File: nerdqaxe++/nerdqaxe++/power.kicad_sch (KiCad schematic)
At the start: 60 parts, among them J3 Conn_01x01, J4 Conn_01x01, U3 TPS53647, U36 MCP1824T-1202E, U6 AP3211, U7 MCP1824T-0802E

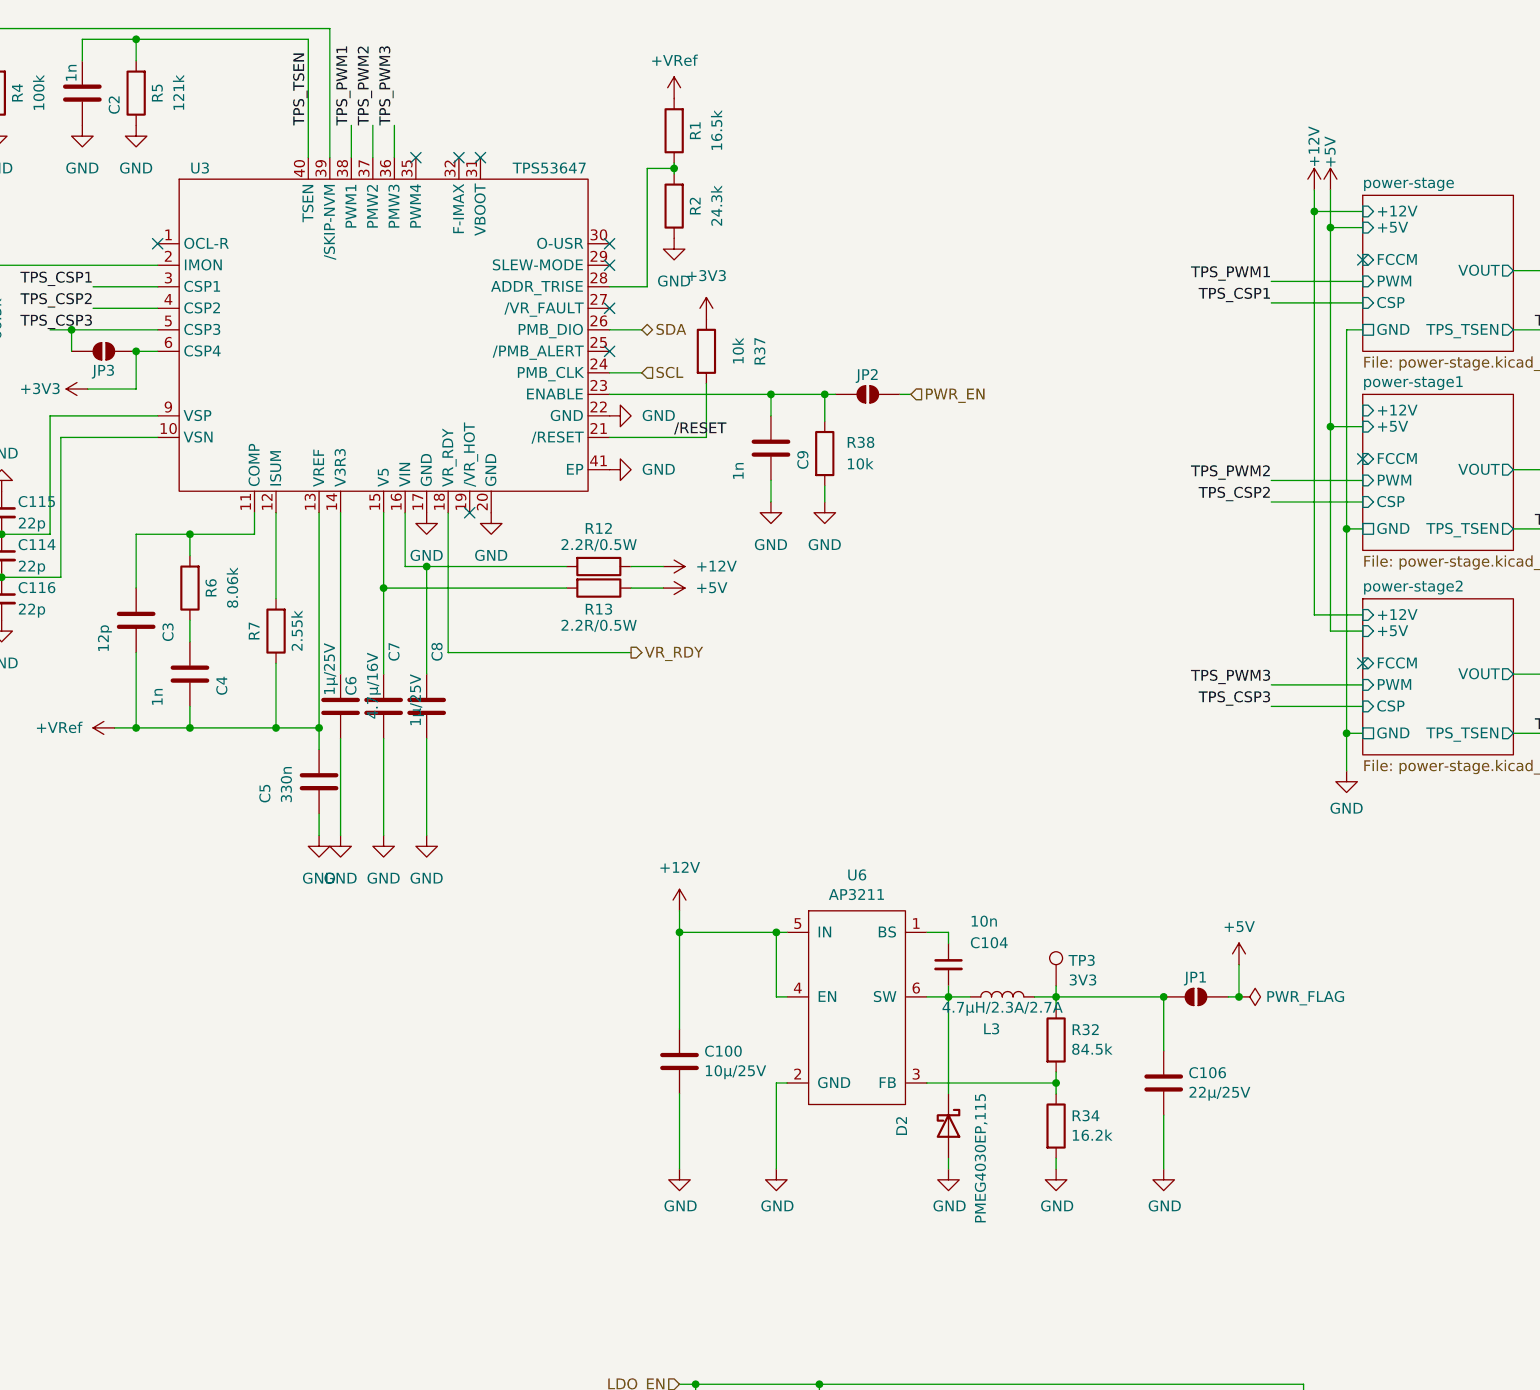
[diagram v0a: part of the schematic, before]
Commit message: Updated PCB layout
- Replaced barrel jack socket with XT30M
- Replaced old fuse holder with new 3568
- Reordered components for AP3211 5V buck converter
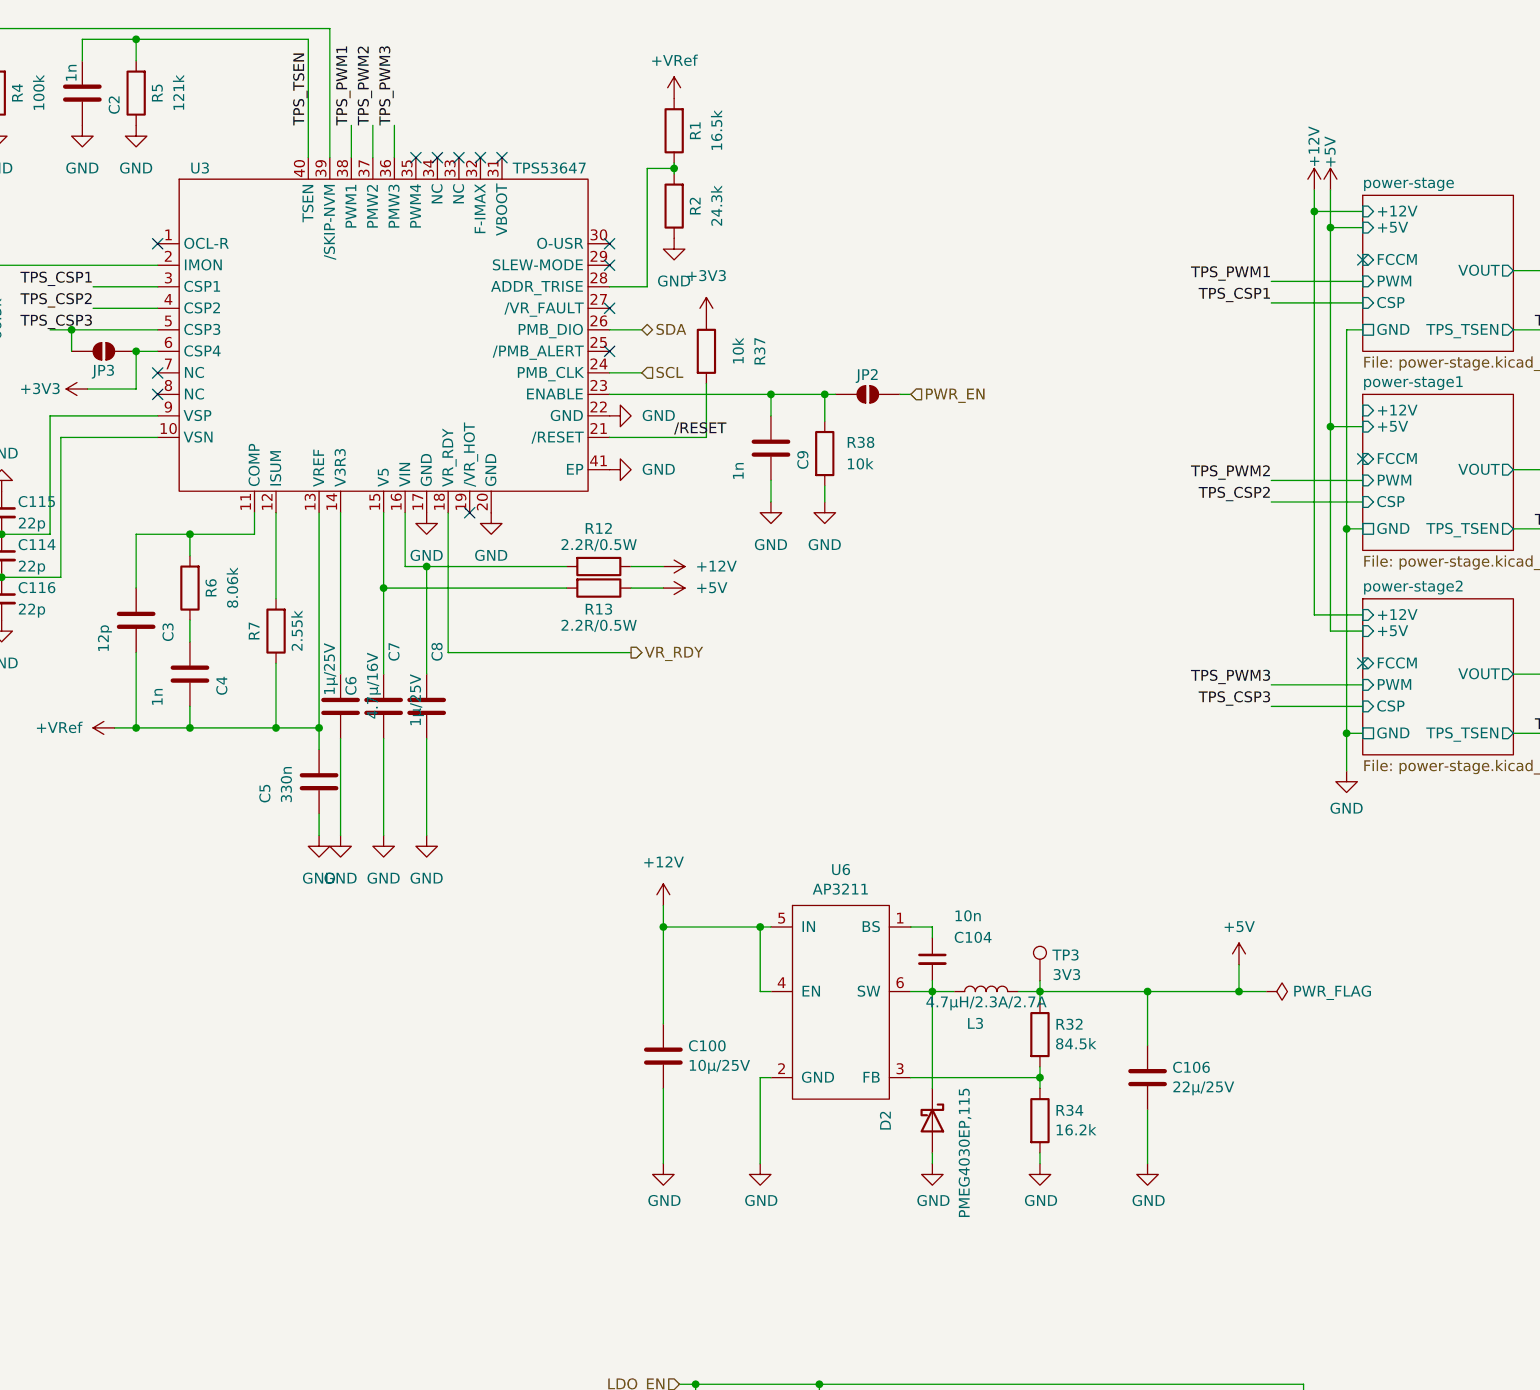
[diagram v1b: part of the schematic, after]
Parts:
- removed JP1: SolderJumper_2_Open, Jumper:SolderJumper-2_P1.3mm_Open_RoundedPad1.0x1.5mm, symbol Jumper:SolderJumper_2_Open
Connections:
- net +5V: now also C106.1, L3.2, R32.1, TP3.1
- no-connect marks 14 -> 18
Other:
- moved on the sheet: C100, C104, C106, D2, L3, R32, R34, TP3, U6

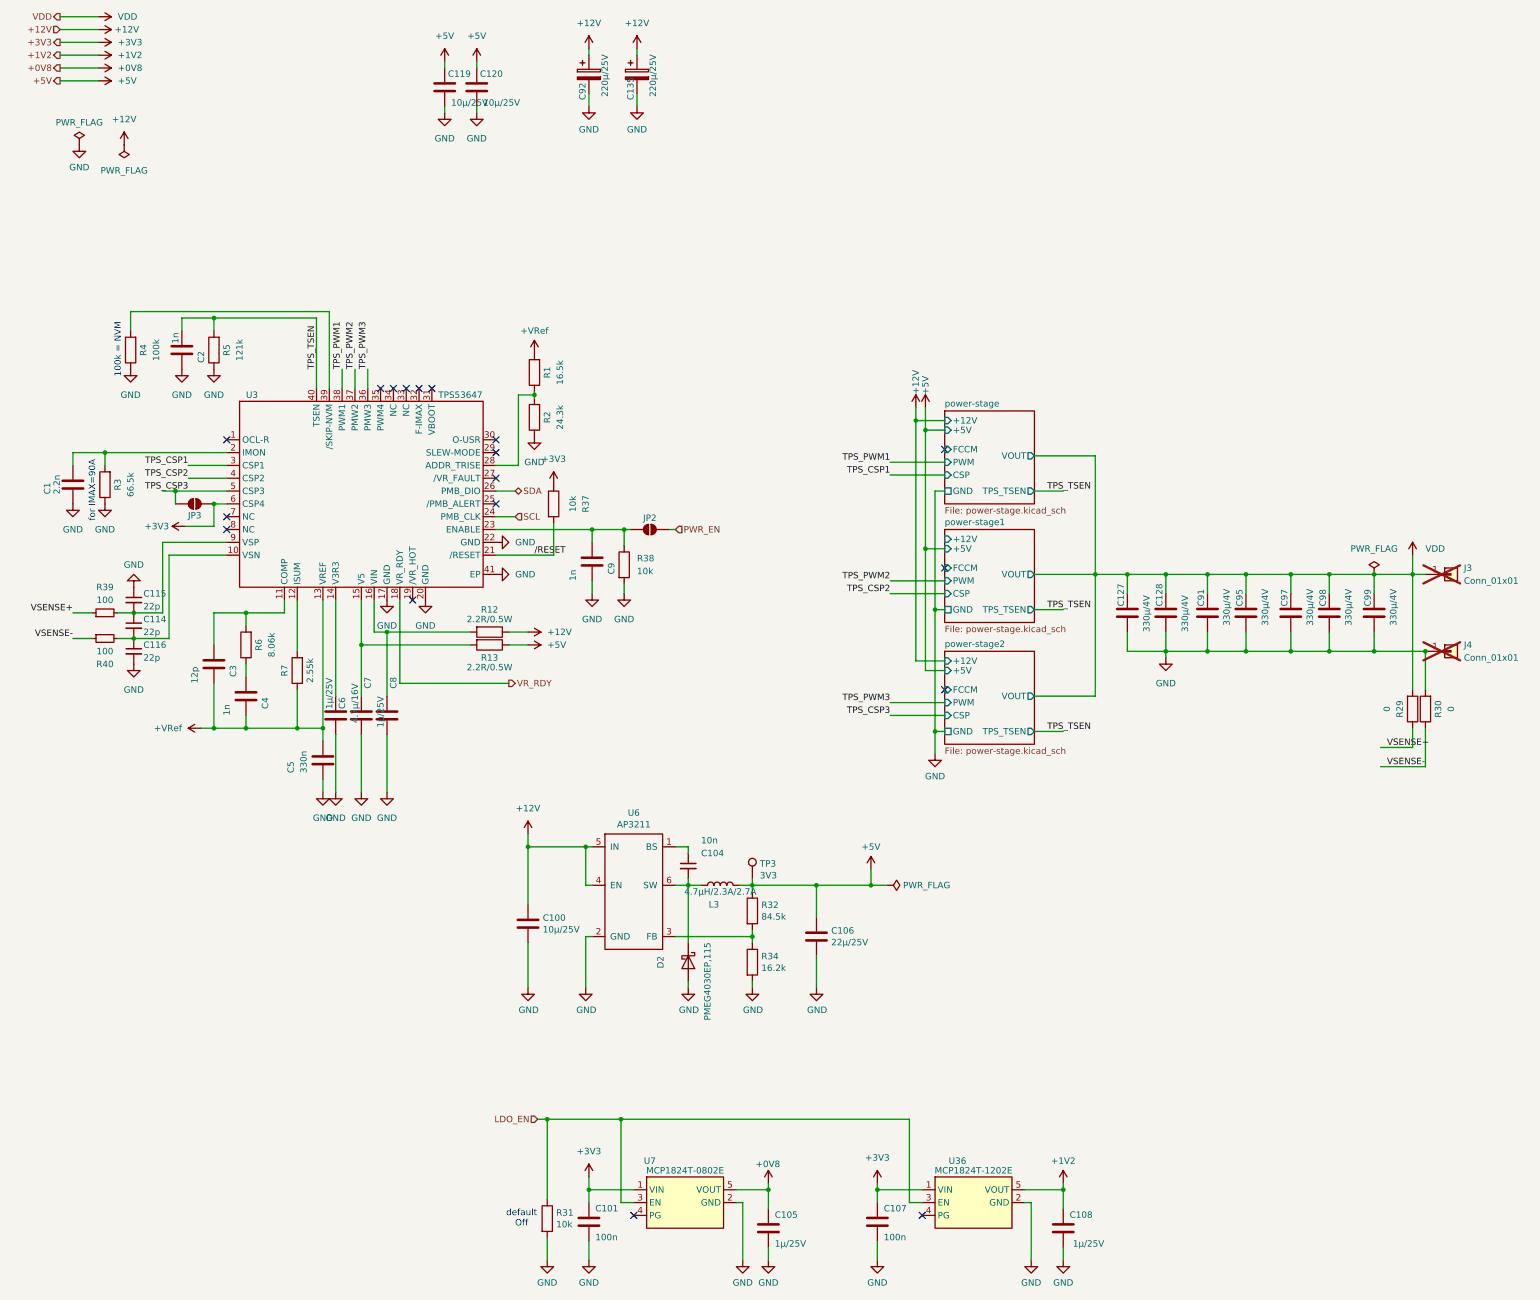
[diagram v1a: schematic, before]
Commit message: Nerdqaxe++ rev6.1.2PM
1. BM1370 Footprint solder paste revision
2. Added 2R2 resistor in series with bootstrap cap for CSD95472Q5MC
3. 180nH inductors for CSD
4. Vsense closer to ASICs
5. Fiducials
6. Updated top silkscreen
7. Various changes in tracing
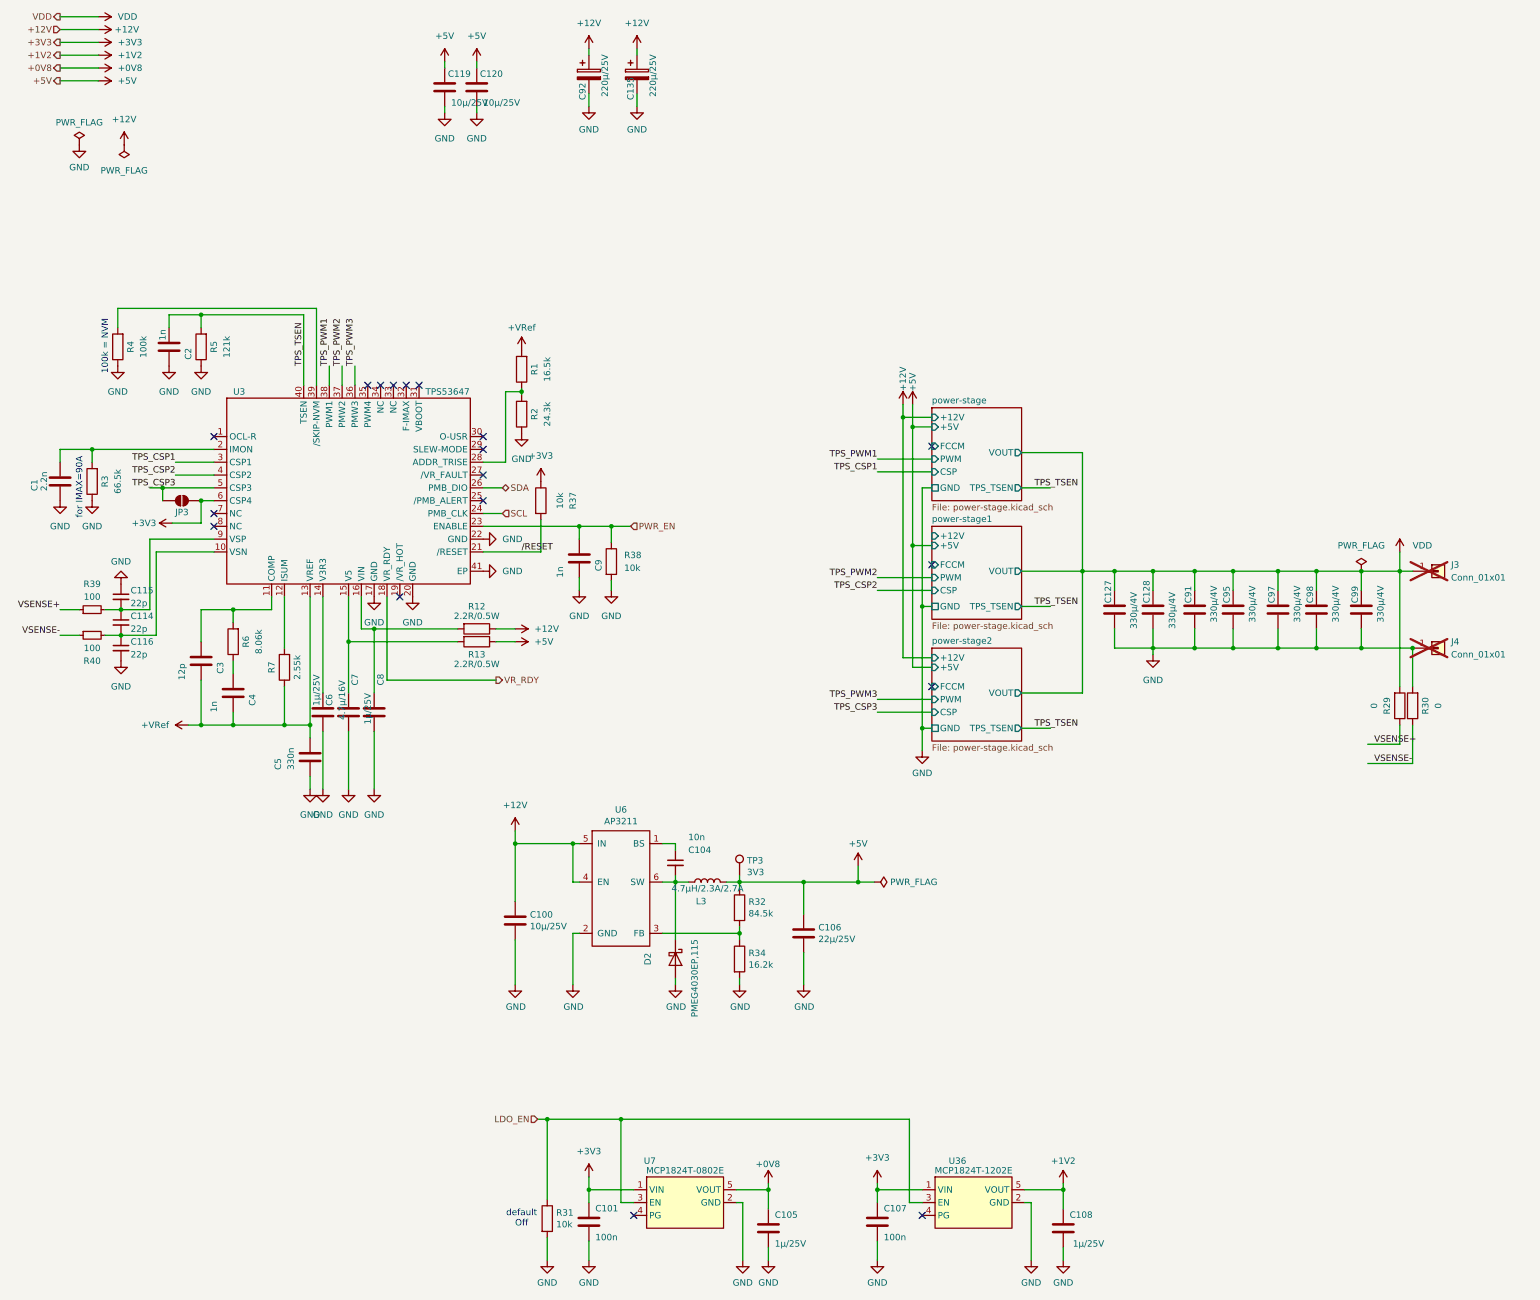
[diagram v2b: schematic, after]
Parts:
- removed JP2: SolderJumper_2_Open, Jumper:SolderJumper-2_P1.3mm_Open_RoundedPad1.0x1.5mm, symbol Jumper:SolderJumper_2_Open
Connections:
- net PWR_EN: now also C9.1, R38.1, U3.23 (ENABLE)
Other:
- moved on the sheet: C1, C100, C104, C106, C114, C115, C116, C127, C128, C2, C3, C4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
